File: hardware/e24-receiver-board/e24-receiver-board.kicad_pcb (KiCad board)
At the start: 2 copper layers, 24 x 8.6 mm, 21 parts, among them J1 505070-2422, J10 SPEAKER-, J11 GND1, J12 TRACK_RIGHT, J13 MOTOR+, J14 LAMP_REAR, J15 CAP+, J16 U+, J17 AUX3, J18 AUX10, J19 AUX12, J2 TRACK_LEFT, J20 SPEAKER+, J21 GND2, J3 MOTOR-, J4 LAMP_FRONT, J5 VCC, J6 AUX1, J7 AUX2, J8 AUX4, J9 AUX11

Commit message: chore: add hardware revision and date codes
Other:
- board text added: "${REVISION}"
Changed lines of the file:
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@@
 	)
 	(paper "A4")
+	(title_block
+		(date "2025-02-02")
+		(rev "v0.1.0")
+	)
 	(layers
 		(0 "F.Cu" signal)
@@
 	)
 	(gr_text "E24 Adapter"
-		(at 143.74 70.61 0)
+		(at 143.25 69.85 0)
 		(layer "B.SilkS")
 		(effects
@@
 		)
 	)
+	(gr_text "${REVISION}"
+		(at 143.25 70.95 0)
+		(layer "B.SilkS")
+		(effects
+			(font
+				(size 1 1)
+				(thickness 0.2)
+				(bold yes)
+			)
+			(justify mirror)
+		)
+	)

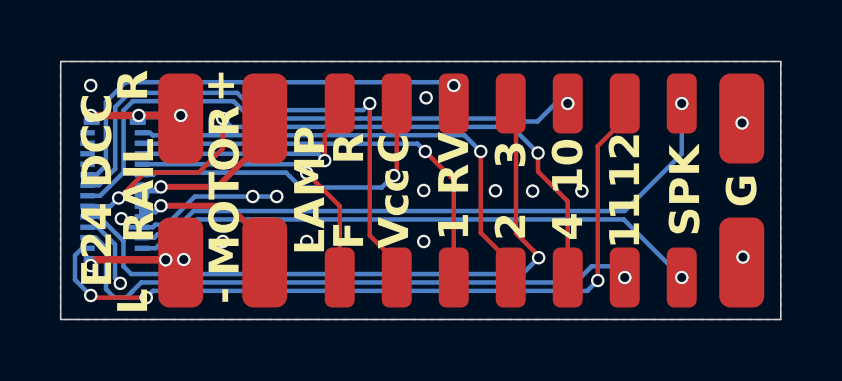
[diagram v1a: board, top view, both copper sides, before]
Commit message: fix: update to kicad 9.0
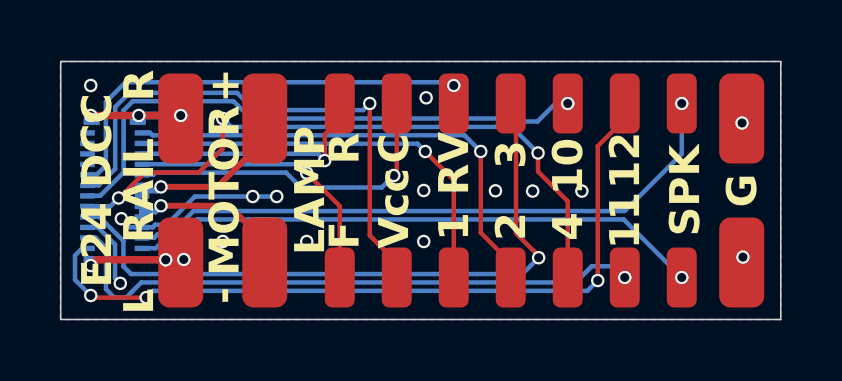
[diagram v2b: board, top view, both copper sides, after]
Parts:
- J1: footprint Local Library:5050702422 -> e24-receiver-board:CONN-SMD_24P-P0.35_5050702422
- J10, J14, J15, J16, J17, J18, J19, J20, J4, J5, J6, J7, J8, J9: footprint Connector_Wire:SolderWirePad_1x01_SMD_1x2mm -> e24-receiver-board:SolderWirePad_1x01_SMD_1x2mm
- J11, J12, J13, J2, J21, J3: footprint Local Library:SolderWirePad_1x01_SMD_1.5x3mm -> e24-receiver-board:SolderWirePad_1x01_SMD_1.5x3mm
